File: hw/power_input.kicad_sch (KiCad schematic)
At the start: 23 parts, among them Q101 SQD50P08-25L, Q102 IPD90N10S4-06, U101 TLV3201, U102 UCC27517A

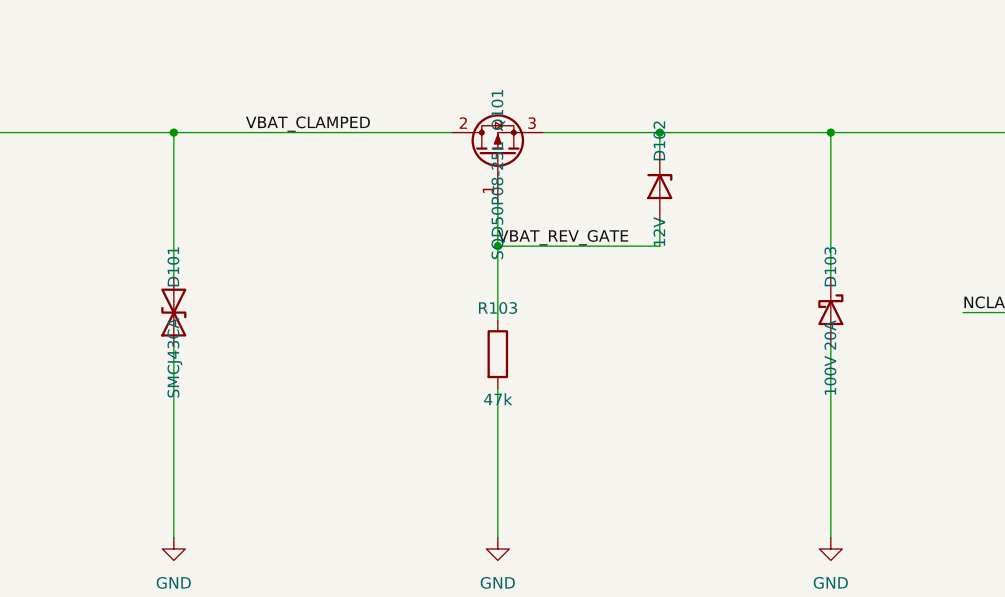
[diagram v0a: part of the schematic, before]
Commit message: Choose the diodes; the boost VDD clamp was 10 V over its pin rating
Part numbers for 27 diodes, each against a retrieved datasheet, applied
through one table (schlib.CHOSEN) keyed by symbol and class value, so
the class stays on the part as a field:
  VS-16EDH02HM3 x7   injector recirculation / blocking / freewheel
  VS-2EMH02HM3       boost diode
  VS-1EMH02HM3 x8    bootstrap and relay flyback
  VS-3ECH02HM3       metering freewheel
  SS20PH102HM3       negative-clamp backstop Schottky
  SMCJ43CA-HM3, SMAJ48CA-HE3, BZX84-C12-Q x2, BZX84-C13-Q, BZG03C36-HM3

The TPS40210 VDD clamp had been checked as an ideal 43.0 V source
behind 47 ohm. The real part in that class (40-46 V, +0.12 %/K, 45 ohm)
puts 61.9 V on a 52 V pin at 125 C, and its 40 V minimum conducts on
the load dump it was chosen to avoid. Now 220 ohm -- which the chosen
switch's gate charge allows -- and a 36 V zener: 46.6 V worst case with
tolerance, tempco and impedance, 33 mA on the dump. 39 V was tried
first; the transient_clamp rail table rejected it at 1.05x. The old
design stays as a pinned check.

TO-277A and SOT-23 zeners put the cathode on pad 3. gen_footprints.py
derives renumbered copies into lib/ecu25kva.pretty (new fp-lib-table).
The GATE_KILL zener, footprinted in the previous commit with the stock
SOT-23, had been reversed.

Left open as LOWV-CLAMP: the 15 zeners at 3.0 and 3.3 V. At tens of uA
a sub-5 V zener's knee is soft -- the datasheet allows 10 uA at 1 V --
and the model's sharp-knee zener hides it.

24/24 sim blocks, netlist gate passing, 74 of 297 parts with footprints.
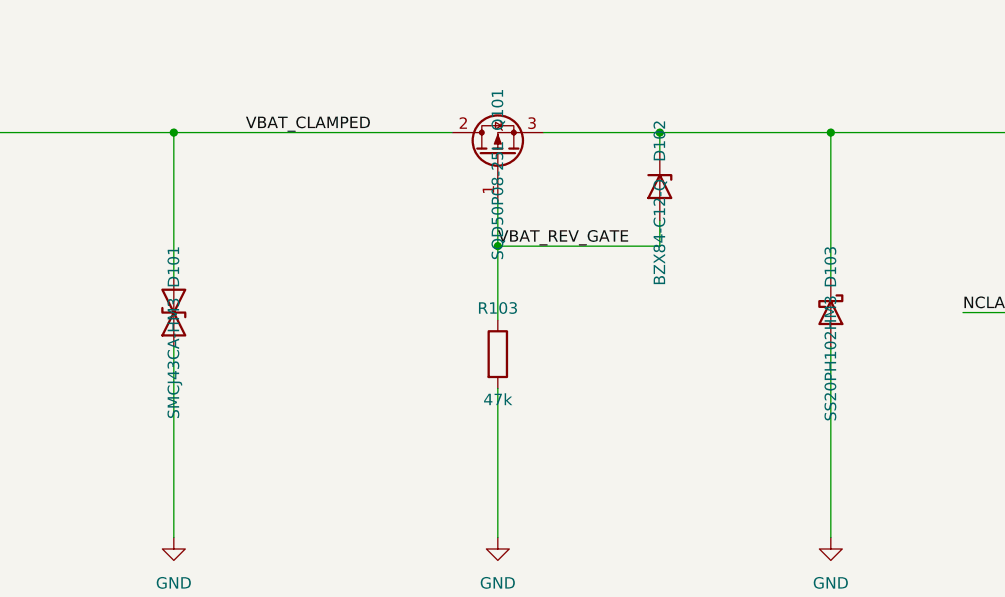
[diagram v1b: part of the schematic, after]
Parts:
- D101: value SMCJ43CA -> SMCJ43CA-HM3; footprint (none) -> Diode_SMD:D_SMC; Chosen (none) -> Vishay TransZorb, 43 V standoff, VBR 47.8-52.8 V, VC 69.4 V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; Class (none) -> SMCJ43CA
- D102: value 12V -> BZX84-C12-Q; footprint (none) -> ecu25kva:SOT-23_Zener_K1_A2; Chosen (none) -> Nexperia BZX84-Q, 11.4-12.7 V at 5 mA, AEC-Q101; Class (none) -> 12V; MPN (none) -> BZX84-C12-Q
- D103: value 100V 20A -> SS20PH102HM3; footprint (none) -> ecu25kva:TO-277A_K1_A2; Chosen (none) -> Vishay TMBS, 100 V, 20 A, 310 A surge, AEC-Q101 (HM3). TO-2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; Class (none) -> 100V 20A; MPN (none) -> SS20PH102HM3
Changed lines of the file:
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@@
       (effects (font (size 1.27 1.27)))
     )
-    (property "Value" "SMCJ43CA" (id 1) (at 232 105.08 0)
-      (effects (font (size 1.27 1.27)))
-    )
-    (property "Footprint" "" (id 2) (at 232 100.0 0)
+    (property "Value" "SMCJ43CA-HM3" (id 1) (at 232 105.08 0)
+      (effects (font (size 1.27 1.27)))
+    )
+    (property "Footprint" "Diode_SMD:D_SMC" (id 2) (at 232 100.0 0)
       (effects (font (size 1.27 1.27)) hide)
     )
@@
       (effects (font (size 1.27 1.27)) hide)
     )
-    (property "Source" "bom_requirements TVS; load_dump.cir, transient_clamp.cir" (id 4) (at 232 100.0 0)
-      (effects (font (size 1.27 1.27)) hide)
-    )
-    (property "MPN" "SMCJ43CA" (id 5) (at 232 100.0 0)
-      (effects (font (size 1.27 1.27)) hide)
-    )
-    (property "Note" "43 V standoff clears the 40 V clamped dump; 1500 W package clamps pulse 2a at 73.3 V vs the buck's 100 V max" (id 6) (at 232 100.0 0)
-      (effects (font (size 1.27 1.27)) hide)
-    )
-    (property "Rotation" "bidirectional -- orientation not significant" (id 7) (at 232 100.0 0)
+    (property "MPN" "SMCJ43CA" (id 4) (at 232 100.0 0)
+      (effects (font (size 1.27 1.27)) hide)
+    )
+    (property "Class" "SMCJ43CA" (id 5) (at 232 100.0 0)
+      (effects (font (size 1.27 1.27)) hide)
+    )
+    (property "Chosen" "Vishay TransZorb, 43 V standoff, VBR 47.8-52.8 V, VC 69.4 V at 21.6 A, 1500 W, AEC-Q101" (id 6) (at 232 100.0 0)
+      (effects (font (size 1.27 1.27)) hide)
+    )
+    (property "Source" "bom_requirements TVS; load_dump.cir, transient_clamp.cir" (id 7) (at 232 100.0 0)
+      (effects (font (size 1.27 1.27)) hide)
+    )
+    (property "Note" "43 V standoff clears the 40 V clamped dump; 1500 W package clamps pulse 2a at 73.3 V vs the buck's 100 V max" (id 8) (at 232 100.0 0)
+      (effects (font (size 1.27 1.27)) hide)
+    )
+    (property "Rotation" "bidirectional -- orientation not significant" (id 9) (at 232 100.0 0)
       (effects (font (size 1.27 1.27)) hide)
     )
@@
       (effects (font (size 1.27 1.27)))
     )
-    (property "Value" "12V" (id 1) (at 286.0 91.08 0)
-      (effects (font (size 1.27 1.27)))
-    )
-    (property "Footprint" "" (id 2) (at 286.0 86.0 0)
+    (property "Value" "BZX84-C12-Q" (id 1) (at 286.0 91.08 0)
+      (effects (font (size 1.27 1.27)))
+    )
+    (property "Footprint" "ecu25kva:SOT-23_Zener_K1_A2" (id 2) (at 286.0 86.0 0)
       (effects (font (size 1.27 1.27)) hide)
     )
@@
       (effects (font (size 1.27 1.27)) hide)
     )
-    (property "Note" "Cathode to SOURCE, anode to GATE: clamps Vgs at -12 V, inside a P-FET's +/-20 V rating, whatever the rail does." (id 4) (at 286.0 86.0 0)
+    (property "MPN" "BZX84-C12-Q" (id 4) (at 286.0 86.0 0)
+      (effects (font (size 1.27 1.27)) hide)
+    )
+    (property "Class" "12V" (id 5) (at 286.0 86.0 0)
+      (effects (font (size 1.27 1.27)) hide)
+    )
+    (property "Chosen" "Nexperia BZX84-Q, 11.4-12.7 V at 5 mA, AEC-Q101" (id 6) (at 286.0 86.0 0)
+      (effects (font (size 1.27 1.27)) hide)
+    )
+    (property "Note" "Cathode to SOURCE, anode to GATE: clamps Vgs at -12 V, inside a P-FET's +/-20 V rating, whatever the rail does." (id 7) (at 286.0 86.0 0)
       (effects (font (size 1.27 1.27)) hide)
     )
@@
       (effects (font (size 1.27 1.27)))
     )
-    (property "Value" "100V 20A" (id 1) (at 305 105.08 0)
-      (effects (font (size 1.27 1.27)))
-    )
-    (property "Footprint" "" (id 2) (at 305 100.0 0)
+    (property "Value" "SS20PH102HM3" (id 1) (at 305 105.08 0)
+      (effects (font (size 1.27 1.27)))
+    )
+    (property "Footprint" "ecu25kva:TO-277A_K1_A2" (id 2) (at 305 100.0 0)
       (effects (font (size 1.27 1.27)) hide)
     )
@@
       (effects (font (size 1.27 1.27)) hide)
     )
-    (property "Source" "bom_requirements NEG-CLAMP (backstop); negative_pulses.cir Dneg1" (id 4) (at 305 100.0 0)
-      (effects (font (size 1.27 1.27)) hide)
-    )
-    (property "Note" "Carries 13.58 A peak / 14.5 mJ on ISO 7637-2 pulse 1. Instant, passive -- holds the node while the comparator decides. Cathode to VIN, anode to ground." (id 5) (at 305 100.0 0)
-      (effects (font (size 1.27 1.27)) hide)
-    )
-    (property "Vr" "100 V class. It was 60 V until 22 Sep 2026: rated for the negative pulse it exists to catch, and not for pulse 2a pushing the SAME node to +73.3 V in reverse." (id 6) (at 305 100.0 0)
-      (effects (font (size 1.27 1.27)) hide)
-    )
-    (property "Ipk" "13.58 A measured" (id 7) (at 305 100.0 0)
-      (effects (font (size 1.27 1.27)) hide)
-    )
+    (property "MPN" "SS20PH102HM3" (id 4) (at 305 100.0 0)
+      (effects (font (size 1.27 1.27)) hide)
+    )
+    (property "Class" "100V 20A" (id 5) (at 305 100.0 0)
+      (effects (font (size 1.27 1.27)) hide)
+    )
+    (property "Chosen" "Vishay TMBS, 100 V, 20 A, 310 A surge, AEC-Q101 (HM3). TO-277A renumbered so the cathode tab is pad 1 -- see gen_footprints.py" (id 6) (at 305 100.0 0)
+      (effects (font (size 1.27 1.27)) hide)
+    )
+    (property "Source" "bom_requirements NEG-CLAMP (backstop); negative_pulses.cir Dneg1" (id 7) (at 305 100.0 0)
+      (effects (font (size 1.27 1.27)) hide)
+    )
+    (property "Note" "Carries 13.58 A peak / 14.5 mJ on ISO 7637-2 pulse 1. Instant, passive -- holds the node while the comparator decides. Cathode to VIN, anode to ground." (id 8) (at 305 100.0 0)
+      (effects (font (size 1.27 1.27)) hide)
+    )
+    (property "Vr" "100 V class. It was 60 V until 22 Sep 2026: rated for the negative pulse it exists to catch, and not for pulse 2a pushing the SAME node to +73.3 V in reverse." (id 9) (at 305 100.0 0)
+      (effects (font (size 1.27 1.27)) hide)
+    )
+    (property "Ipk" "13.58 A measured" (id 10) (at 305 100.0 0)
+      (effects (font (size 1.27 1.27)) hide)
+    )

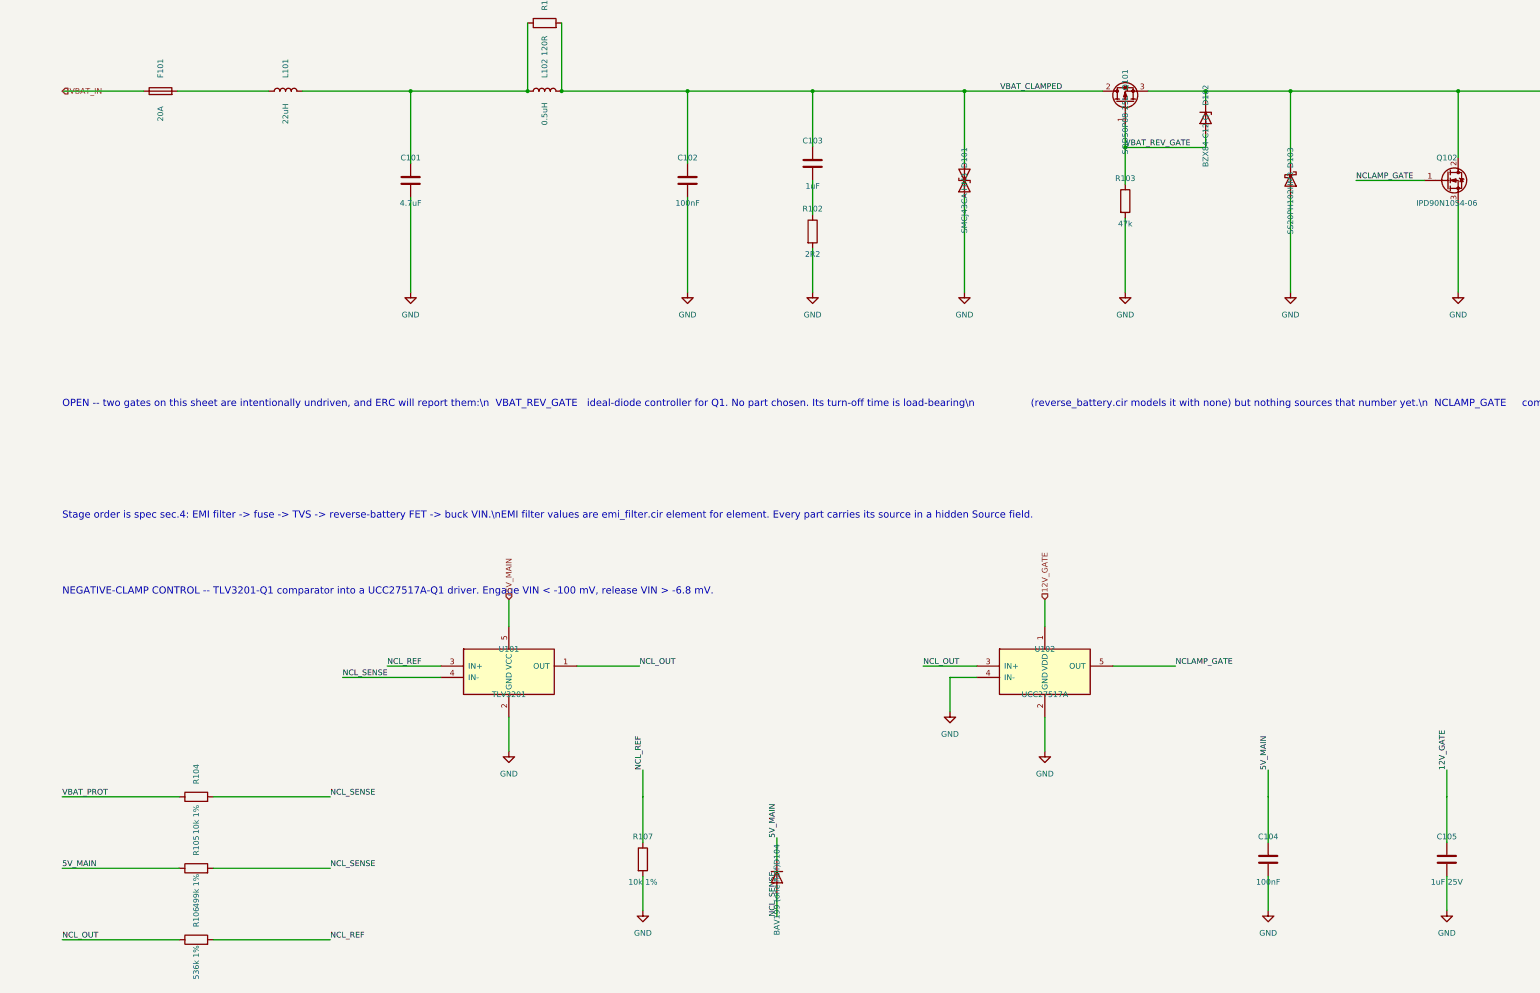
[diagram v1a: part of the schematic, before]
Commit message: Package every resistor and capacitor from the voltage across it
hw/assign_passives.py sizes all 188 chip R and C from a per-net table
of continuous and peak voltage (73.3 V pulse 2a, 104 V boost, bootstrap
domains riding on the bank nodes), against Vishay CRCW e3 resistor
ratings (Umax with 1.09x margin, power derated to 0.588x at a 105 C
board) and KEMET's automotive X7R waterfall (parsed by x-coordinate;
the text layout misreads its columns). schlib.place() applies the map
by ref and value; check_netlist fails on any unpackaged R or C.

Found along the way:
- 4.7 uF at 100 V is not in automotive X7R. The EMI filter C1, buck
  input and boost input are now 2 x 2.2 uF 100 V 1210; emi_filter.cir
  models the pair and its cold corner was re-pinned (0.6 dB worse).
- The twelve 470 ohm gate pulldowns need 2010: 0.31 W each at 100%
  duty. Recorded; 1k may now be possible against the real Crss.
- Local labels at 180 degrees were justified in the wrong frame on
  every sheet -- the bug fixed for hierarchical labels earlier -- so
  their text sat across their own wire. Fixed in schlib.label().

Internal nodes whose voltage matters now carry names (FB_BOOST_MID,
CAN1_SPLIT, ...); auto-names like Net-(R407-Pad2) move when parts are
added ahead of them.

24/24 sim blocks, netlist gate passing, 264 of 302 parts footprinted.
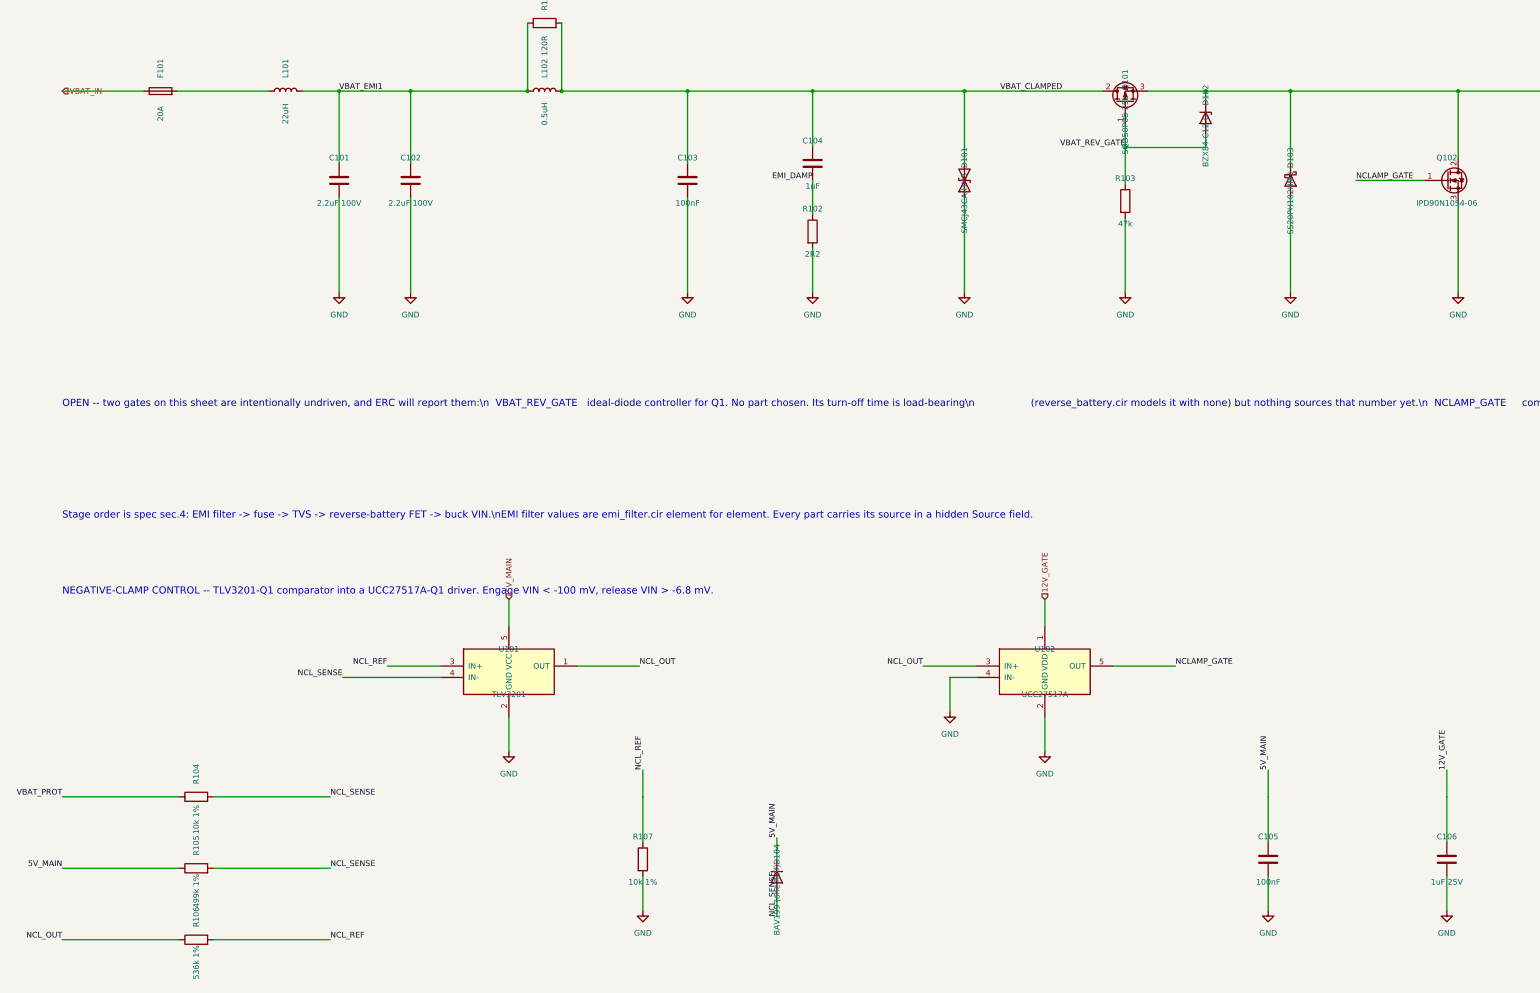
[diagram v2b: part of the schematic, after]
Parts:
- added C106: 1uF 25V, Capacitor_SMD:C_0805_2012Metric, symbol Device:C
- C101: value 4.7uF -> 2.2uF 100V; footprint (none) -> Capacitor_SMD:C_1210_3225Metric; ESR 5 mOhm max -> 5 mOhm max each; Source emi_filter.cir C1 -- ESR 5 mOhm, ESL 1.5 nH modelled -> emi_filter.cir C1 -- one of two in parallel
- C102: value 100nF -> 2.2uF 100V; footprint (none) -> Capacitor_SMD:C_1210_3225Metric; ESR 20 mOhm max -> 5 mOhm max each; Source emi_filter.cir C2 -- ESR 20 mOhm, ESL 0.5 nH modelled -> emi_filter.cir C1 -- one of two in parallel
- C103: value 1uF -> 100nF; footprint (none) -> Capacitor_SMD:C_0603_1608Metric; ESR (none) -> 20 mOhm max; Source emi_filter.cir Cd -- damping leg, series with Rd -> emi_filter.cir C2 -- ESR 20 mOhm, ESL 0.5 nH modelled
- C104: value 100nF -> 1uF; footprint (none) -> Capacitor_SMD:C_1206_3216Metric; Note Comparator bypass. -> (none); Source (none) -> emi_filter.cir Cd -- damping leg, series with Rd
- C105: value 1uF 25V -> 100nF; footprint (none) -> Capacitor_SMD:C_0603_1608Metric; Note Driver bypass -- it sources 4 A peak into the clamp FET's g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 -> Comparator bypass.
- R101, R102, R105, R106, R107: footprint (none) -> Resistor_SMD:R_0603_1608Metric
- R103, R104: footprint (none) -> Resistor_SMD:R_0805_2012Metric
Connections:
- net 12V_GATE: now also C106.1; no longer C105.1
- net 5V_MAIN: now also C105.1; no longer C104.1
- net GND: now also C103.2, C106.2; no longer C104.2
- net VBAT_CLAMPED: now also C104.1; no longer C102.1
- net VBAT_EMI1: now reaches C101.1, L101.2, L102.1, R101.1
- net VBAT_EMI1: now also C102.1
- net EMI_DAMP: now reaches R102.1
- net EMI_DAMP: now also C104.2; no longer C103.2
